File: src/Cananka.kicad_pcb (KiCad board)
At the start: 2 copper layers, 105.8 x 26 mm, 55 parts, among them J1 USB4085 B1HSW6, J2 MC 1,5/4, Q1 DMP3085, Q2 BSS84, U1 FT230XS, U2 PIC18F25K80, U3 ISO1050, U4 74LVC1T45, Y1 12 MHz

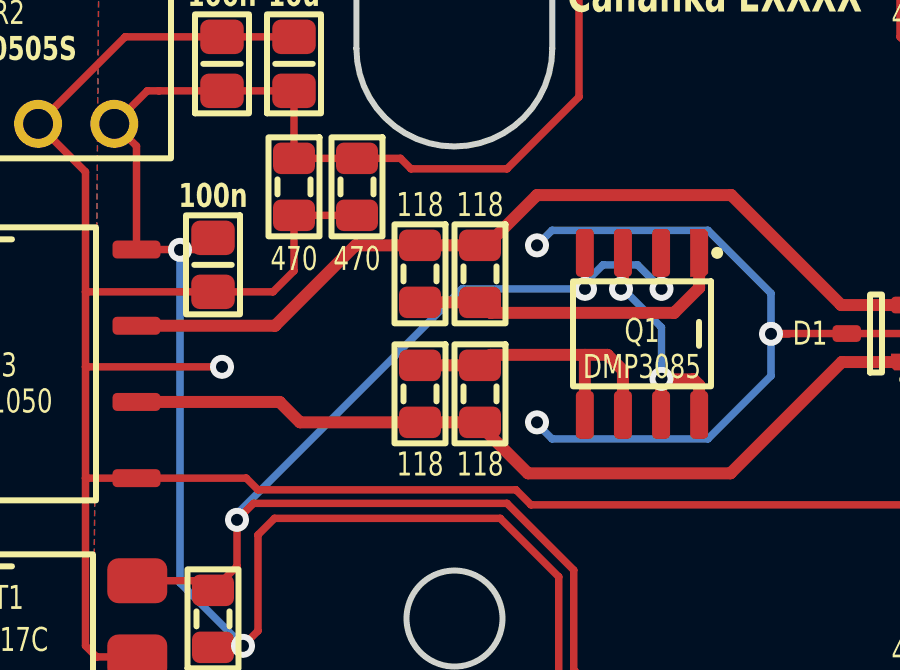
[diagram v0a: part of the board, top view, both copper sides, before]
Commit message: Increasing termination resistor value
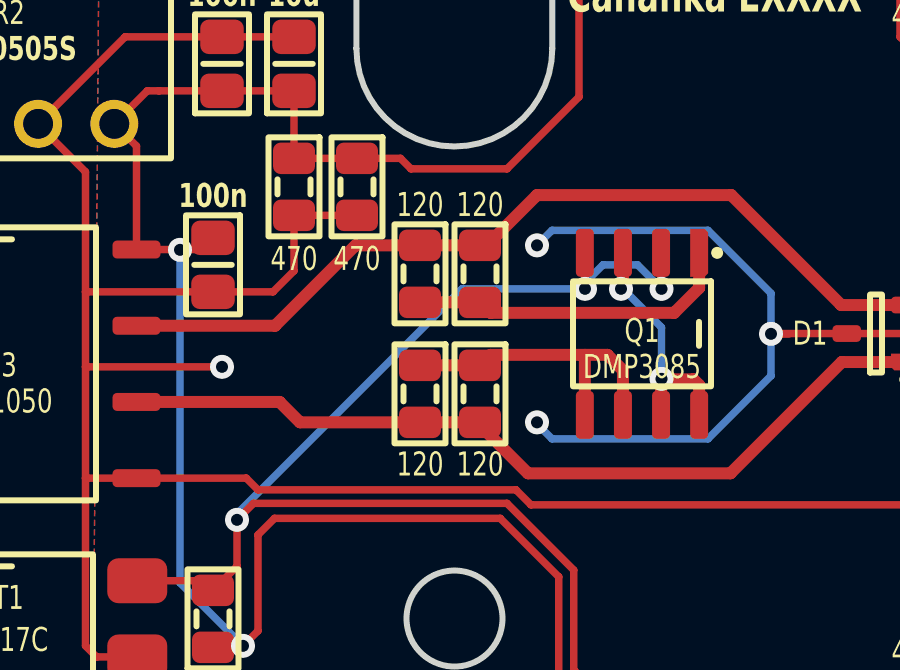
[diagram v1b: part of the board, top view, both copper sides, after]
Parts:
- R3, R4, R5, R6: value 118 -> 120
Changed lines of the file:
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@@
 			)
 		)
-		(property "Value" "118"
+		(property "Value" "120"
 			(at -2.3 0 0)
 			(layer "F.SilkS")
@@
 			)
 		)
-		(property "Value" "118"
+		(property "Value" "120"
 			(at 2.35 0 0)
 			(layer "F.SilkS")
@@
 			)
 		)
-		(property "Value" "118"
+		(property "Value" "120"
 			(at -2.3 0 0)
 			(layer "F.SilkS")
@@
 			)
 		)
-		(property "Value" "118"
+		(property "Value" "120"
 			(at 2.35 0 0)
 			(layer "F.SilkS")
